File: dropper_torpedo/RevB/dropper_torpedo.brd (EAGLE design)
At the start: 76.2 x 50.8 mm, 72 parts, among them CON1 SM03B-GHS-TB, CON2 SM03B-GHS-TB, CON3 MOLEX_5566-2, CON4 MOLEX_5566-2, CON6 MOLEX_5566-2, Q1 SI4896DY-T1-E3, Q2 SI4896DY-T1-E3, Q3 IRL6372TRPBF, Q4 IRL6372TRPBF, U1 LTV-355T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

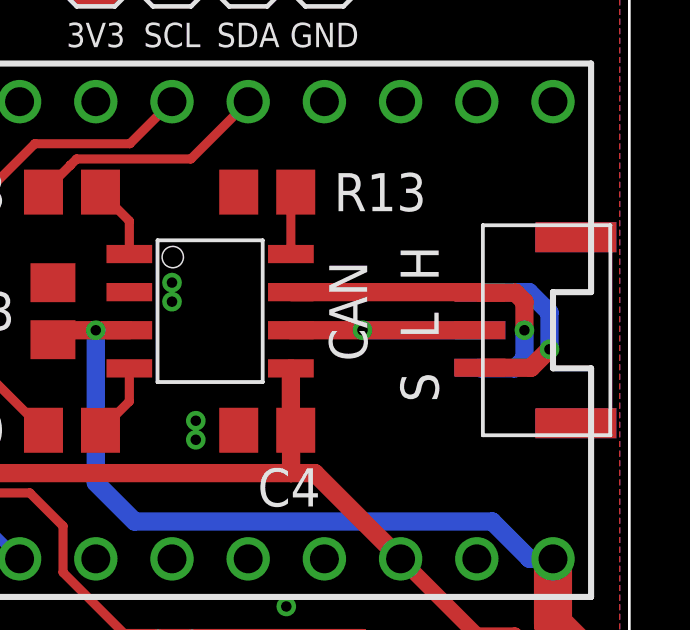
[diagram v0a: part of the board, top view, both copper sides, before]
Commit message: dropper_torpedo: swapped out 3 pin JST for standards-based 4-pin
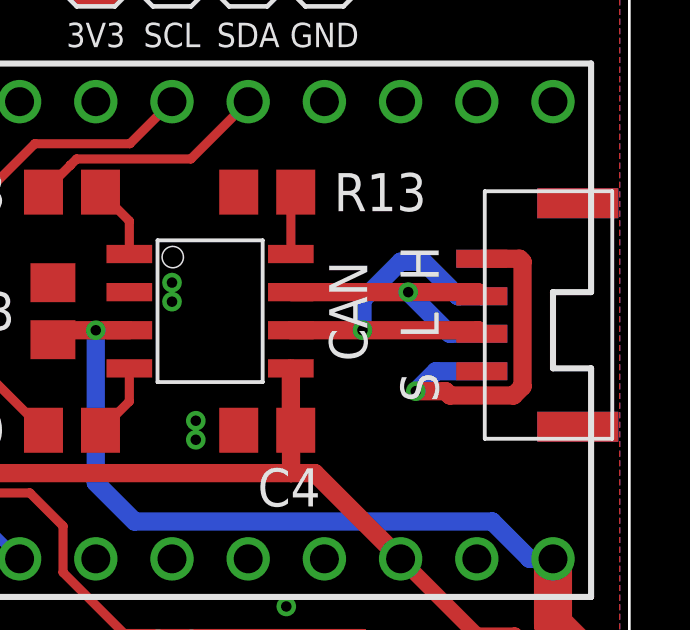
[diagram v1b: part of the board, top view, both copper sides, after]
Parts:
- CON1, CON2: value SM03B-GHS-TB -> SM04B-GHS-TB; device ARVP:SM03B-GHS-TB -> ARVP:SM04B-GHS-TB
- moved CON1 0.51 mm to (72.1, 34.8)
- moved CON2 0.51 mm to (72.1, 34.8)
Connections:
- removed net CANSH: CON1.P$1, CON2.P$1
- new net +5V_CAN: CON1.P$4, CON2.P$4
- net GND: now also CON1.P$1, CON1.P$6, CON2.P$1, CON2.P$6; no longer CON1.P$4, CON2.P$4
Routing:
- net +5V_CAN: track 0.00 -> 11.8 mm, vias 0 -> 1
- net CANSH: track 6.41 -> 0.00 mm, vias 1 -> 0
- net CANL: track 10.2 -> 12.4 mm
- net CANH: track 11.4 -> 9.45 mm
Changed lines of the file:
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@@
 <?xml version="1.0" encoding="utf-8"?>
 <!DOCTYPE eagle SYSTEM "eagle.dtd">
-<eagle version="9.5.2">
+<eagle version="9.6.1">
 <drawing>
 <settings>
@@
 <attribute name="VALUE" x="63.5" y="36.35375" size="1.27" layer="27"/>
 </element>
-<element name="CON1" library="ARVP" package="SM03B-GHS-TB" value="SM03B-GHS-TB" x="72.0725" y="34.29" smashed="yes" rot="R90"/>
-<element name="CON2" library="ARVP" package="SM03B-GHS-TB" value="SM03B-GHS-TB" x="72.0725" y="34.29" smashed="yes" rot="MR270"/>
 <element name="R9" library="rcl" library_urn="urn:adsk.eagle:library:334" package="R0805" package3d_urn="urn:adsk.eagle:package:23553/2" value="5k" x="29.845" y="22.38375" smashed="yes">
 <attribute name="VALUE" x="28.575" y="19.84375" size="1.27" layer="27"/>
@@
 <attribute name="VALUE" x="64.77" y="2.794" size="1.27" layer="27" rot="R90"/>
 </element>
+<element name="CON1" library="ARVP" package="SM04B-GHS-TB" value="SM04B-GHS-TB" x="72.136" y="34.798" smashed="yes" rot="R90"/>
+<element name="CON2" library="ARVP" package="SM04B-GHS-TB" value="SM04B-GHS-TB" x="72.136" y="34.798" smashed="yes" rot="MR270"/>
 </elements>
 <signals>
@@
 <contactref element="C3" pad="2"/>
 <contactref element="R13" pad="1"/>
-<contactref element="CON1" pad="P$5"/>
-<contactref element="CON1" pad="P$4"/>
-<contactref element="CON2" pad="P$5"/>
-<contactref element="CON2" pad="P$4"/>
 <via x="61.75375" y="31.27375" extent="1-16" drill="0.35"/>
 <via x="61.75375" y="30.63875" extent="1-16" drill="0.35"/>
@@
 <via x="64.77" y="25.0825" extent="1-16" drill="0.35"/>
 <via x="52.22875" y="44.45" extent="1-16" drill="0.35"/>
+<contactref element="CON2" pad="P$6"/>
+<contactref element="CON2" pad="P$5"/>
+<contactref element="CON1" pad="P$1"/>
+<contactref element="CON2" pad="P$1"/>
+<contactref element="CON1" pad="P$6"/>
+<contactref element="CON1" pad="P$5"/>
 </signal>
 <signal name="+5V">
@@
 <signal name="CANH">
 <contactref element="U3" pad="7"/>
+<contactref element="CON2" pad="P$3"/>
 <contactref element="CON1" pad="P$3"/>
-<contactref element="CON2" pad="P$3"/>
-<wire x1="64.9224" y1="35.56" x2="71.2025" y2="35.56" width="0.6096" layer="1"/>
-<wire x1="71.2025" y1="35.56" x2="71.2225" y2="35.54" width="0.6096" layer="1"/>
-<wire x1="71.2225" y1="35.54" x2="72.41" y2="35.54" width="0.6096" layer="1"/>
-<wire x1="72.41" y1="35.54" x2="72.7075" y2="35.2425" width="0.6096" layer="1"/>
-<wire x1="72.7075" y1="35.2425" x2="72.7075" y2="34.29" width="0.6096" layer="1"/>
-<via x="72.7075" y="34.29" extent="1-16" drill="0.35"/>
-<wire x1="72.7075" y1="34.29" x2="72.7075" y2="33.3375" width="0.6096" layer="16"/>
-<wire x1="72.7075" y1="33.3375" x2="72.39" y2="33.02" width="0.6096" layer="16"/>
-<wire x1="72.39" y1="33.02" x2="71.2425" y2="33.02" width="0.6096" layer="16"/>
-<wire x1="71.2425" y1="33.02" x2="71.2225" y2="33.04" width="0.6096" layer="16"/>
+<wire x1="64.9224" y1="35.56" x2="68.834" y2="35.56" width="0.6096" layer="1"/>
+<wire x1="68.834" y1="35.56" x2="71.149" y2="35.56" width="0.6096" layer="1"/>
+<wire x1="71.149" y1="35.56" x2="71.286" y2="35.423" width="0.6096" layer="1"/>
+<via x="68.834" y="35.56" extent="1-16" drill="0.35"/>
+<wire x1="68.834" y1="35.56" x2="70.221" y2="34.173" width="0.6096" layer="16"/>
+<wire x1="70.221" y1="34.173" x2="71.286" y2="34.173" width="0.6096" layer="16"/>
 </signal>
 <signal name="CANL">
 <contactref element="U3" pad="6"/>
+<wire x1="64.9224" y1="34.29" x2="67.31" y2="34.29" width="0.6096" layer="1"/>
+<via x="67.31" y="34.29" extent="1-16" drill="0.35"/>
+<contactref element="CON2" pad="P$2"/>
 <contactref element="CON1" pad="P$2"/>
-<contactref element="CON2" pad="P$2"/>
-<wire x1="64.9224" y1="34.29" x2="67.31" y2="34.29" width="0.6096" layer="1"/>
-<wire x1="67.31" y1="34.29" x2="71.2225" y2="34.29" width="0.6096" layer="1"/>
-<wire x1="71.2225" y1="34.29" x2="67.31" y2="34.29" width="0.6096" layer="16"/>
-<via x="67.31" y="34.29" extent="1-16" drill="0.35"/>
-</signal>
-<signal name="CANSH">
-<contactref element="CON1" pad="P$1"/>
-<contactref element="CON2" pad="P$1"/>
-<wire x1="71.2225" y1="33.04" x2="72.9279" y2="33.04" width="0.6096" layer="1"/>
-<wire x1="72.9279" y1="33.04" x2="73.5429" y2="33.655" width="0.6096" layer="1"/>
-<via x="73.5429" y="33.655" extent="1-16" drill="0.35"/>
-<wire x1="73.5429" y1="33.655" x2="73.5429" y2="34.88335" width="0.6096" layer="16"/>
-<wire x1="73.5429" y1="34.88335" x2="72.86625" y2="35.56" width="0.6096" layer="16"/>
-<wire x1="72.86625" y1="35.56" x2="71.2425" y2="35.56" width="0.6096" layer="16"/>
-<wire x1="71.2425" y1="35.56" x2="71.2225" y2="35.54" width="0.6096" layer="16"/>
+<wire x1="67.31" y1="34.29" x2="71.169" y2="34.29" width="0.6096" layer="1"/>
+<wire x1="71.169" y1="34.29" x2="71.286" y2="34.173" width="0.6096" layer="1"/>
+<wire x1="67.31" y1="34.29" x2="67.31" y2="35.306" width="0.6096" layer="16"/>
+<wire x1="67.31" y1="35.306" x2="68.58" y2="36.576" width="0.6096" layer="16"/>
+<wire x1="68.58" y1="36.576" x2="69.342" y2="36.576" width="0.6096" layer="16"/>
+<wire x1="70.495" y1="35.423" x2="71.286" y2="35.423" width="0.6096" layer="16"/>
+<wire x1="69.342" y1="36.576" x2="70.495" y2="35.423" width="0.6096" layer="16"/>
 </signal>
 <signal name="TRP1_ALT">
@@
 <contactref element="CON6" pad="2"/>
 </signal>
+<signal name="+5V_CAN">
+<contactref element="CON1" pad="P$4"/>
+<contactref element="CON2" pad="P$4"/>
+<wire x1="71.286" y1="32.923" x2="69.753" y2="32.923" width="0.6096" layer="16"/>
+<wire x1="69.753" y1="32.923" x2="69.088" y2="32.258" width="0.6096" layer="16"/>
+<via x="69.088" y="32.258" extent="1-16" drill="0.35"/>
+<wire x1="70.22558125" y1="32.115" x2="72.34641875" y2="32.115" width="0.6096" layer="1"/>
+<wire x1="72.34641875" y1="32.115" x2="72.644" y2="32.41258125" width="0.6096" layer="1"/>
+<wire x1="69.088" y1="32.258" x2="70.08258125" y2="32.258" width="0.6096" layer="1"/>
+<wire x1="70.08258125" y1="32.258" x2="70.22558125" y2="32.115" width="0.6096" layer="1"/>
+<wire x1="72.644" y1="32.41258125" x2="72.644" y2="36.576" width="0.6096" layer="1"/>
+<wire x1="72.547" y1="36.673" x2="71.286" y2="36.673" width="0.6096" layer="1"/>
+<wire x1="72.644" y1="36.576" x2="72.547" y2="36.673" width="0.6096" layer="1"/>
+</signal>
 </signals>
